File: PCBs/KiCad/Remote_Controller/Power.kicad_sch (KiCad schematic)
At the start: 8 parts

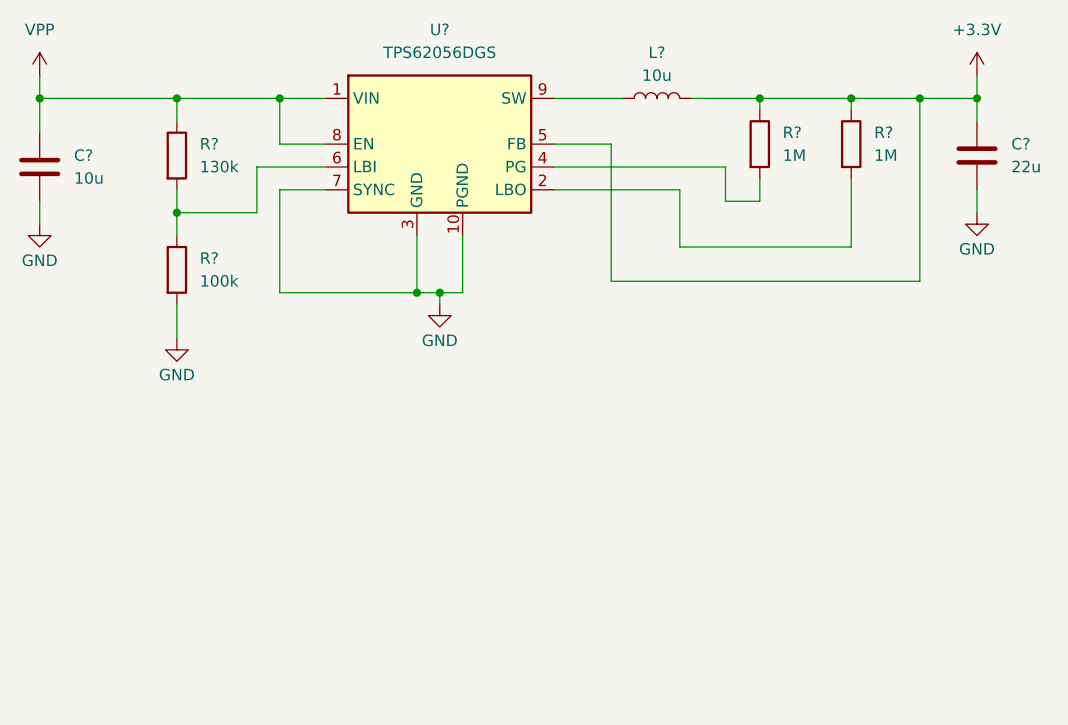
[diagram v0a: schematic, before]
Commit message: Add battery and USB as power sources
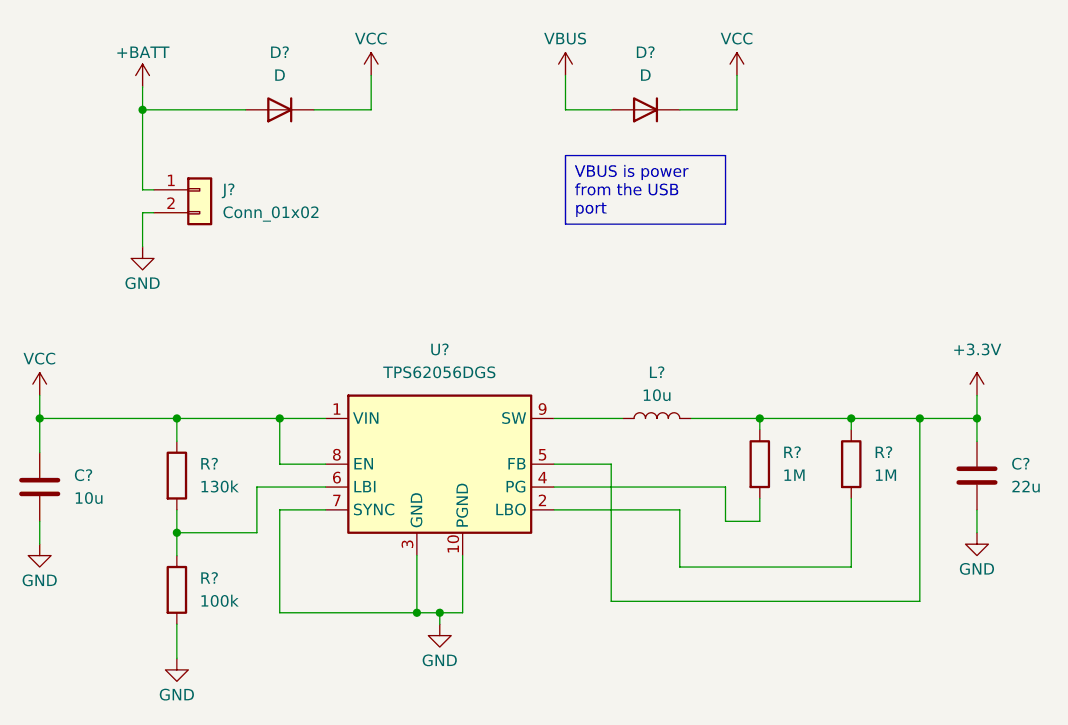
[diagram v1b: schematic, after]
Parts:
- added D? (x2): D, symbol Device:D
- added J?: Conn_01x02, symbol Connector_Generic:Conn_01x02
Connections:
- net GND: now also J?.2 (Pin_2)
- net VPP renamed VCC
- net VCC: now also D?.1 (K), D?.1 (K)
- new net +BATT: D?.2 (A), J?.1 (Pin_1)
- new net VBUS: D?.2 (A)
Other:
- moved on the sheet: C?, L?, R?, U?

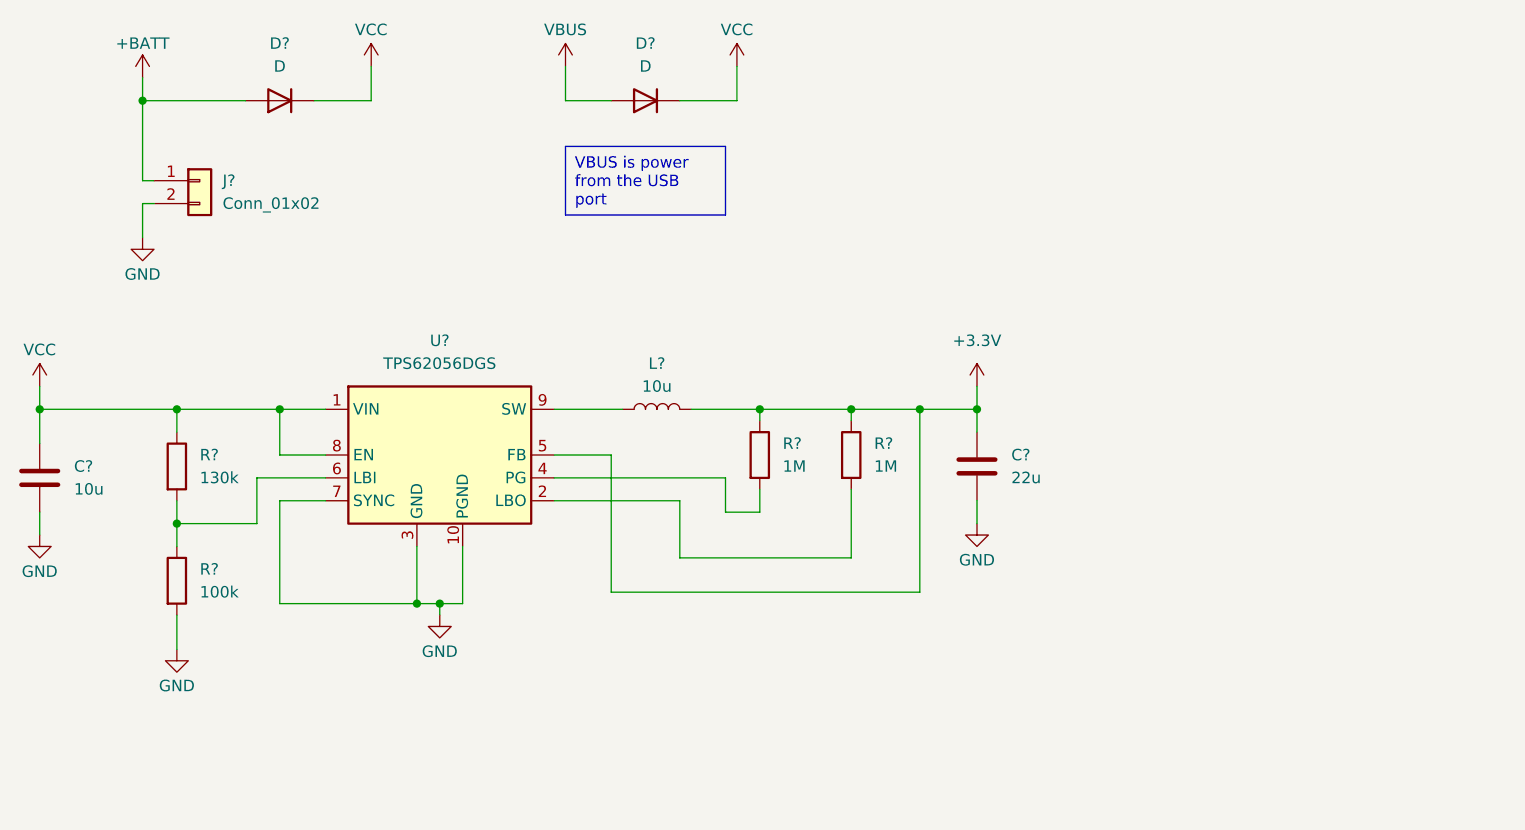
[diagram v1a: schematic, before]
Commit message: Moved project library one folder up to Kicad Folder
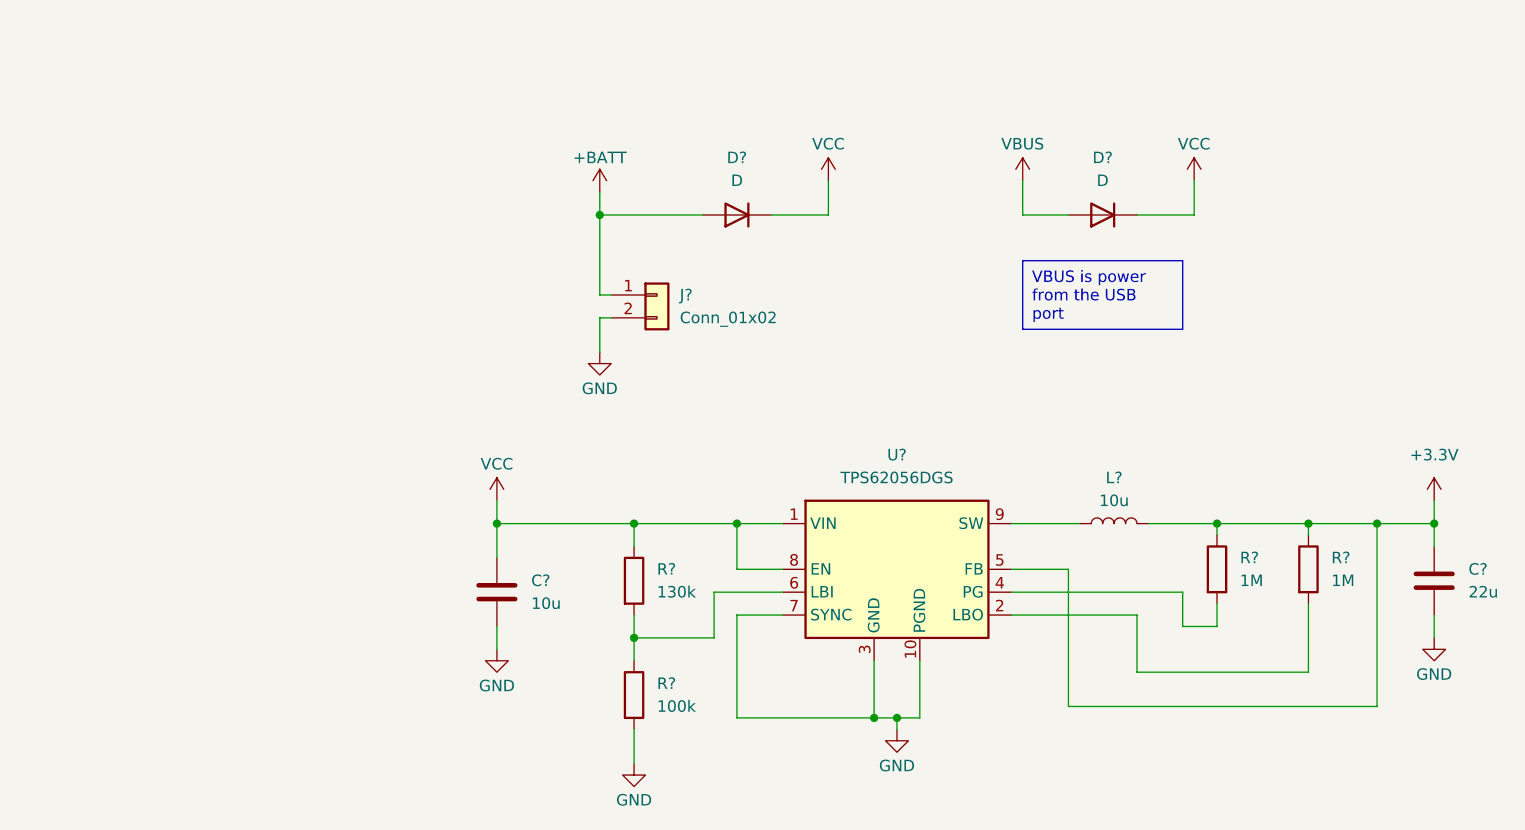
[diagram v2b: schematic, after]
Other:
- moved on the sheet: C?, D?, J?, L?, R?, U?

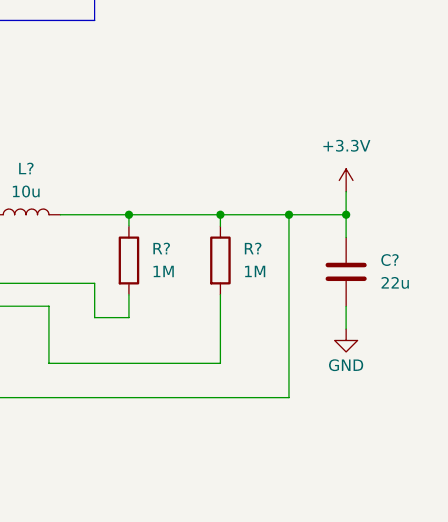
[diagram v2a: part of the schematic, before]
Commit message: Added ESP32-C3-MINI-1 to remote controller
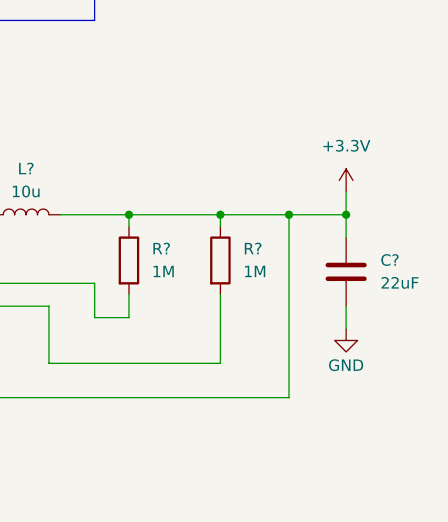
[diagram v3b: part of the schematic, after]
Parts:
- C?: value 22u -> 22uF
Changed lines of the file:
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@@
 			)
 		)
-		(property "Value" "22u"
+		(property "Value" "22uF"
 			(at 196.85 114.2999 0)
 			(effects

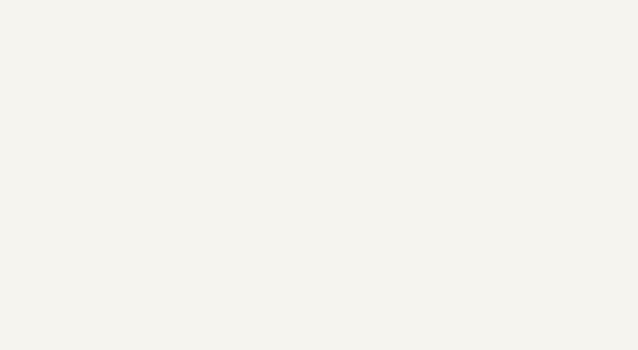
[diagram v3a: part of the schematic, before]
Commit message: Numbered all of the schematics
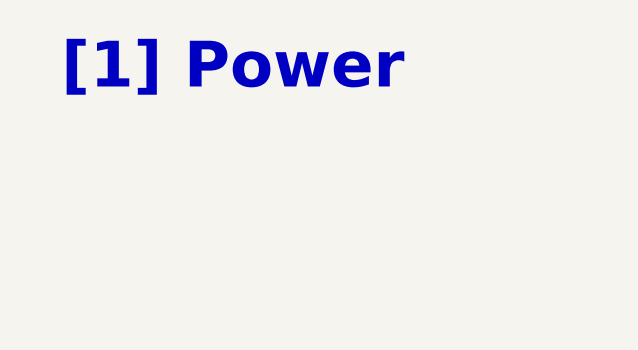
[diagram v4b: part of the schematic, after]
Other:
- note added: "[1] Power"
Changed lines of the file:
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@@
+		)
+	)
+	(text "[1] Power"
+		(exclude_from_sim no)
+		(at 36.322 22.098 0)
+		(effects
+			(font
+				(size 5.08 5.08)
+				(thickness 1.016)
+				(bold yes)
+			)
 		)
 	)

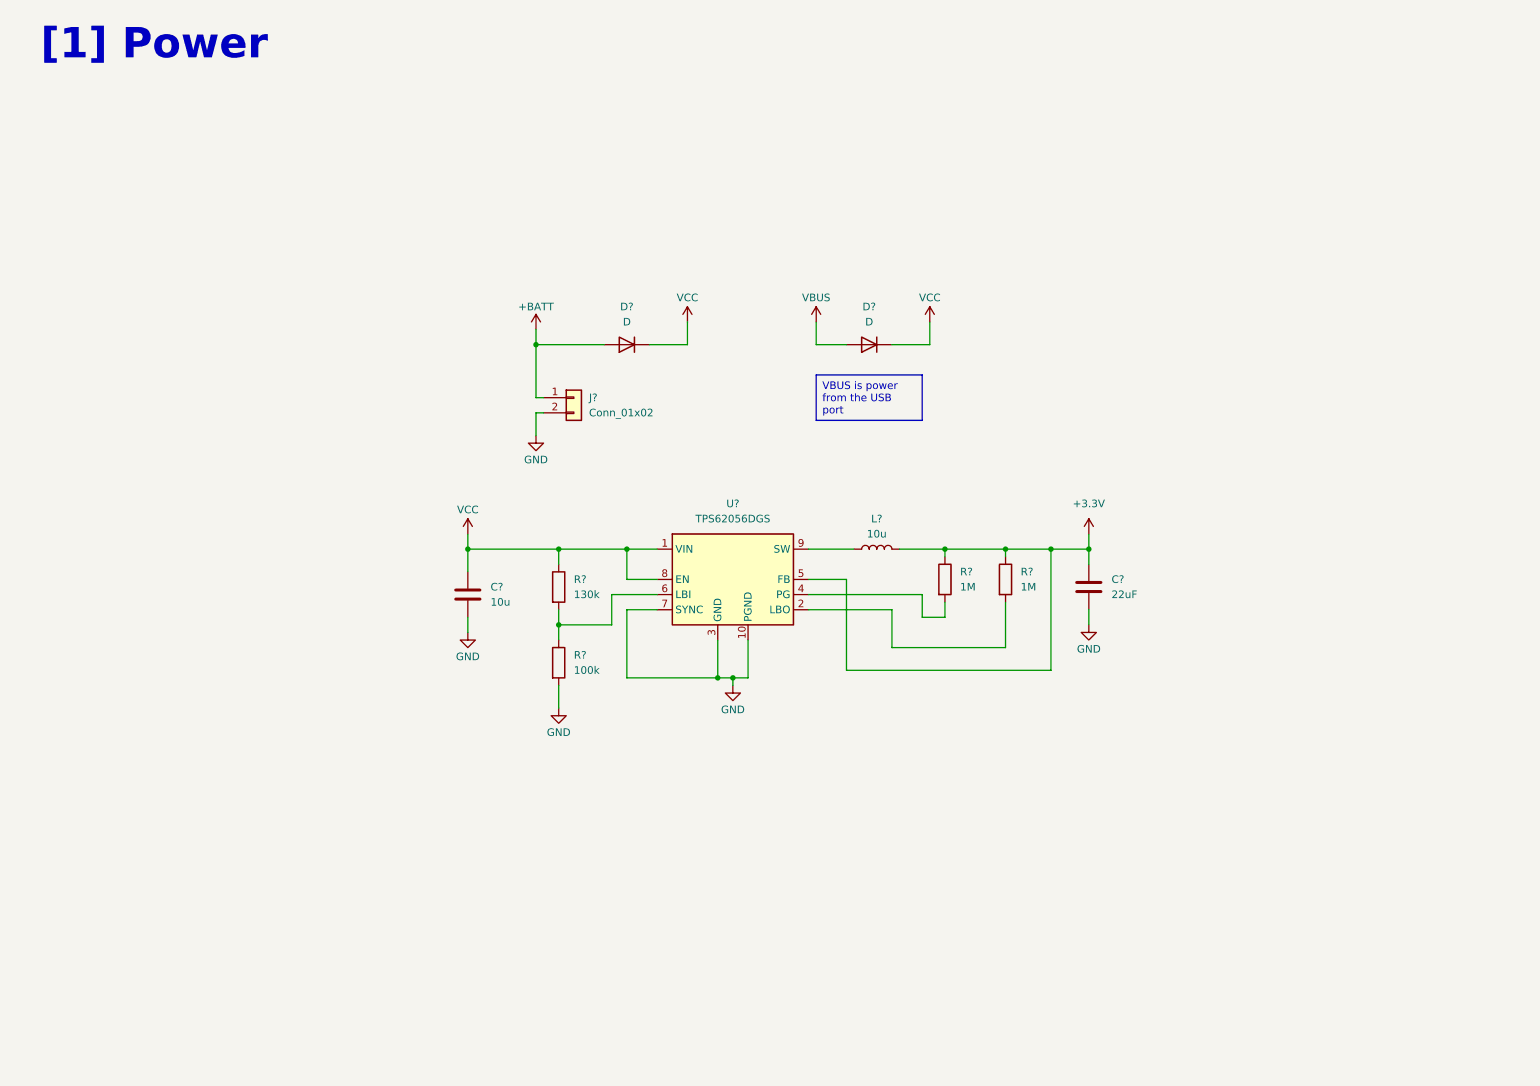
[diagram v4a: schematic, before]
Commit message: Add power multiplexing for 9V battery and USB power
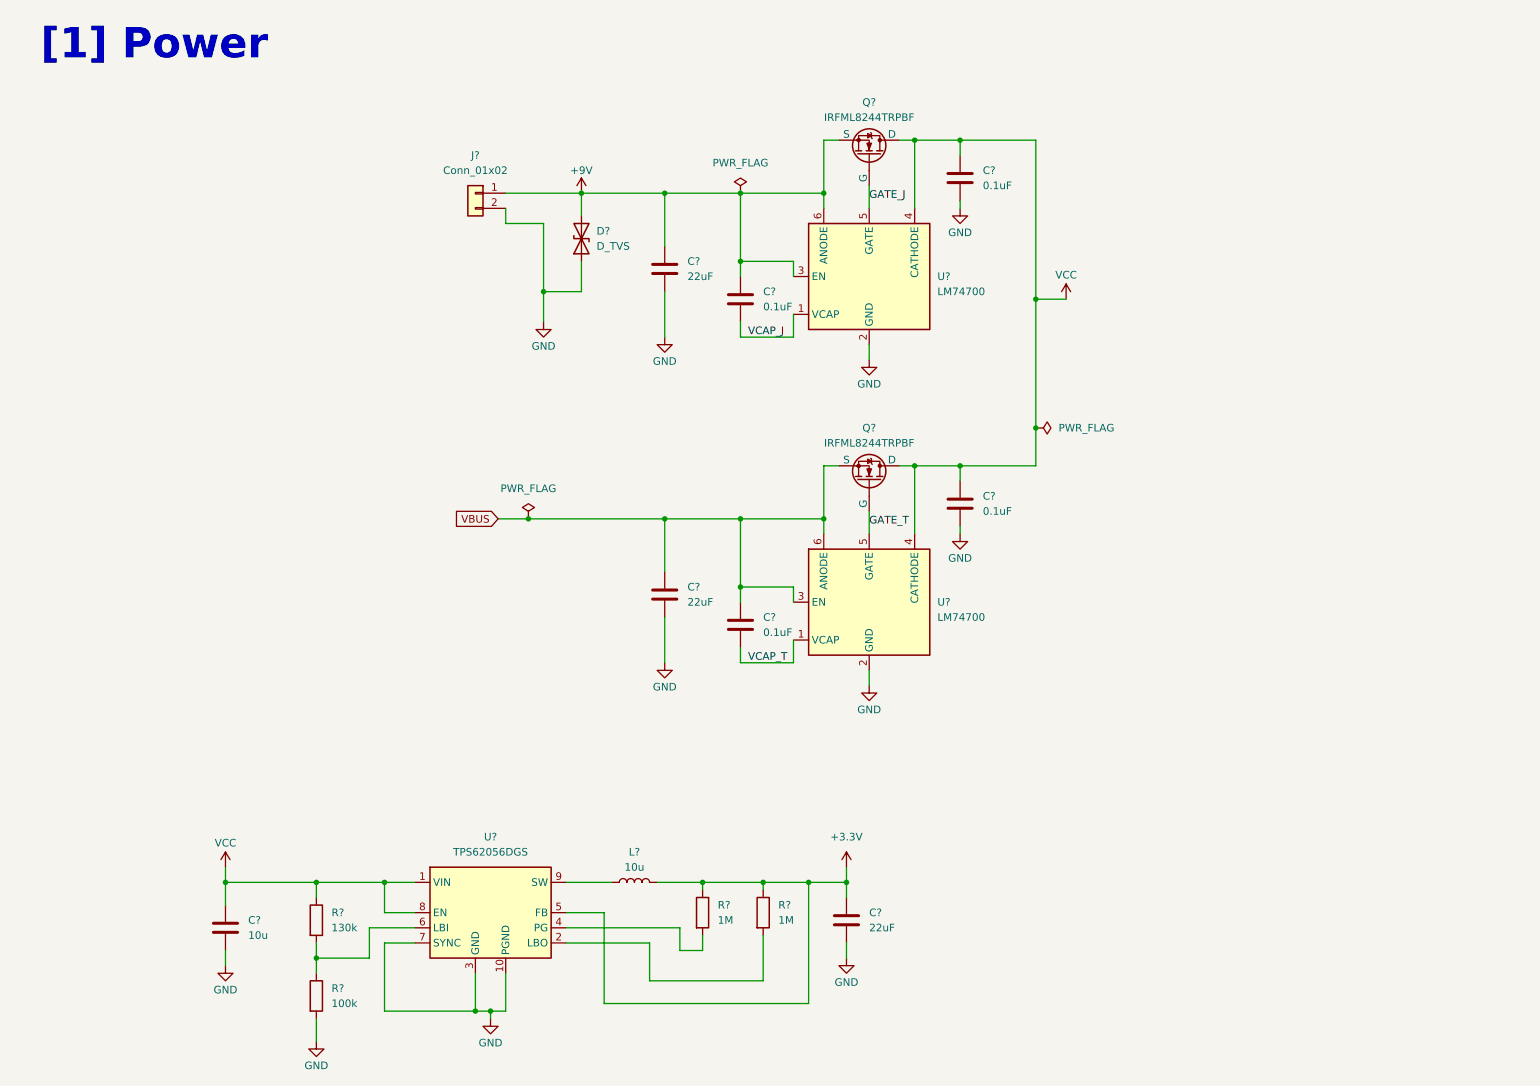
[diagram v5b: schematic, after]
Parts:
- removed D? (x2): D, symbol Device:D
- removed J?: Conn_01x02, symbol Connector_Generic:Conn_01x02
- added C? (x4): 0.1uF, Capacitor_SMD:C_0402_1005Metric, symbol Device:C
- added C? (x2): 22uF, Capacitor_SMD:C_1206_3216Metric, symbol Device:C
- added D?: D_TVS, Diode_SMD:D_SOD-882, symbol Device:D_TVS
- added J?: Conn_01x02, symbol Connector_Generic:Conn_01x02
- added Q? (x2): IRFML8244TRPBF, Package_TO_SOT_SMD:SOT-23, symbol Simulation_SPICE:NMOS
- added U? (x2): LM74700, Package_TO_SOT_SMD:SOT-23-6, symbol Power_Management:LM74700
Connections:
- net GND: now also C?.2, C?.2, C?.2, C?.2, D?.1 (A1), J?.2 (Pin_2), U?.2 (GND), U?.2 (GND)
- net VBUS: now also C?.1, C?.1, Q?.2 (S), U?.3 (EN), U?.6 (ANODE)
- net VCC: now also C?.1, C?.1, Q?.3 (D), Q?.3 (D), U?.4 (CATHODE), U?.4 (CATHODE)
- new net +9V: C?.1, C?.1, D?.2 (A2), J?.1 (Pin_1), Q?.2 (S), U?.3 (EN), U?.6 (ANODE)
- new net GATE_J: Q?.1 (G), U?.5 (GATE)
- new net GATE_T: Q?.1 (G), U?.5 (GATE)
- new net VCAP_J: C?.2, U?.1 (VCAP)
- new net VCAP_T: C?.2, U?.1 (VCAP)
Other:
- moved on the sheet: C?, L?, R?, U?
